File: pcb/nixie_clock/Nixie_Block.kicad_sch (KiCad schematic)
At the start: 25 parts, among them U66 MSD42WT1G, U67 MSD42WT1G, U68 MSD42WT1G, U69 MSD42WT1G, U70 MSD42WT1G, U71 MSD42WT1G, U72 MSD42WT1G, U73 MSD42WT1G, U74 MSD42WT1G, U75 MSD42WT1G, U76 MSD42WT1G, U77 MSD42WT1G

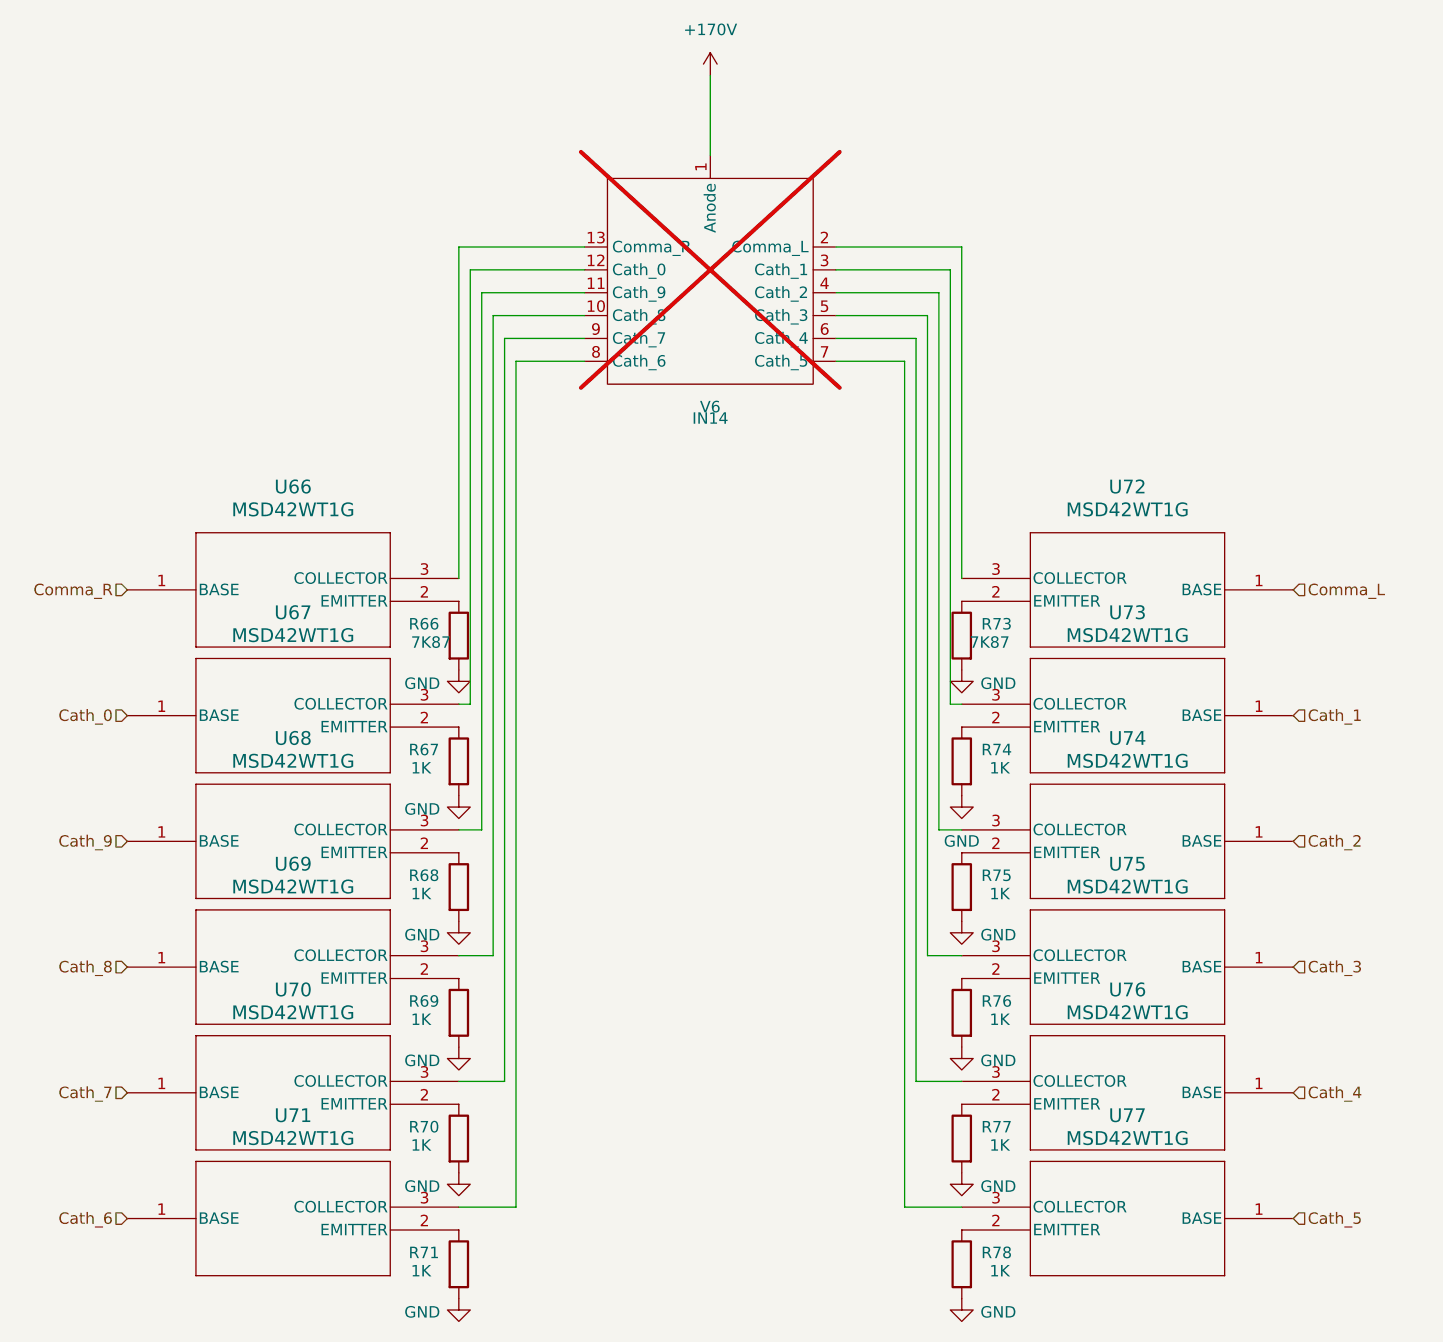
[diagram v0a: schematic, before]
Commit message: pcb changes and breakages need to fix later
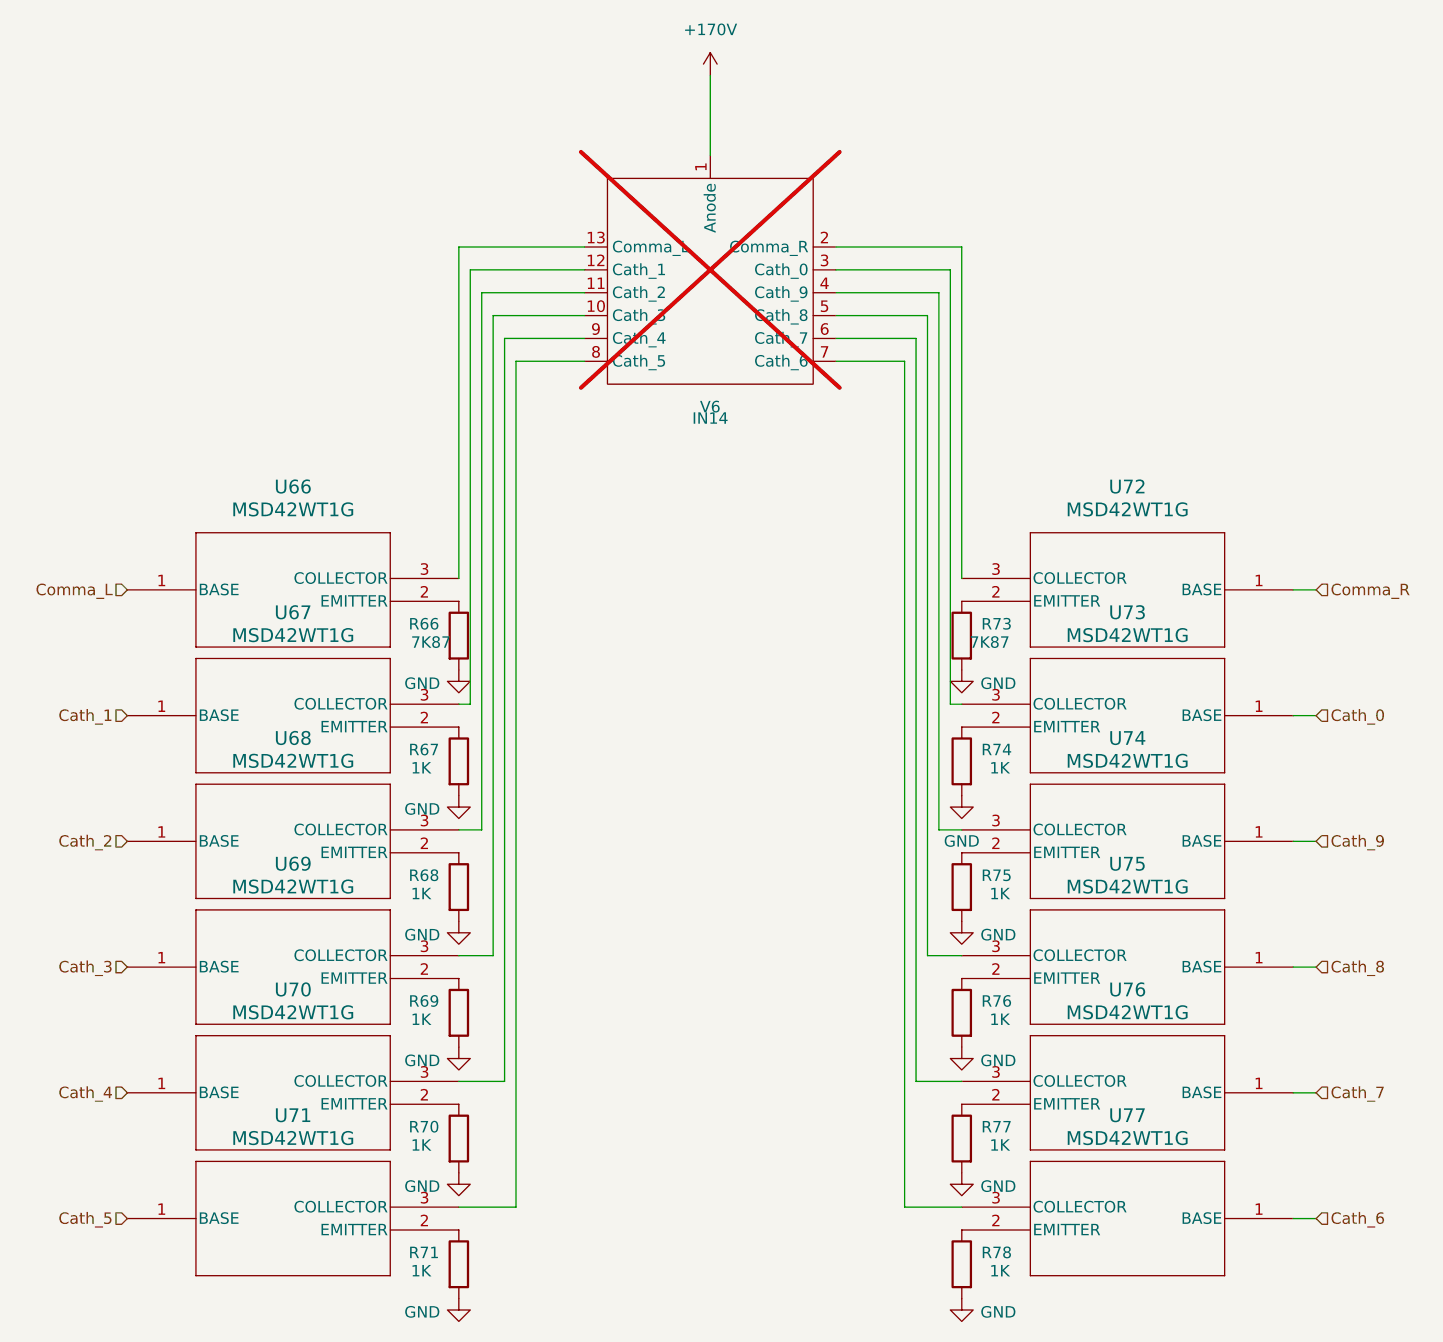
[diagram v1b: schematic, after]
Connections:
- net Cath_0: now also U73.1 (BASE); no longer U67.1 (BASE)
- net Cath_1: now also U67.1 (BASE); no longer U73.1 (BASE)
- net Cath_2: now also U68.1 (BASE); no longer U74.1 (BASE)
- net Cath_3: now also U69.1 (BASE); no longer U75.1 (BASE)
- net Cath_4: now also U70.1 (BASE); no longer U76.1 (BASE)
- net Cath_5: now also U71.1 (BASE); no longer U77.1 (BASE)
- net Cath_6: now also U77.1 (BASE); no longer U71.1 (BASE)
- net Cath_7: now also U76.1 (BASE); no longer U70.1 (BASE)
- net Cath_8: now also U75.1 (BASE); no longer U69.1 (BASE)
- net Cath_9: now also U74.1 (BASE); no longer U68.1 (BASE)
- net Comma_L: now also U66.1 (BASE); no longer U72.1 (BASE)
- net Comma_R: now also U72.1 (BASE); no longer U66.1 (BASE)
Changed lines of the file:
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@@
+	(wire
+		(pts
+			(xy 168.91 133.35) (xy 166.37 133.35)
+		)
+		(stroke
+			(width 0)
+			(type default)
+		)
+	)
 	(wire
 		(pts
@@
 	(wire
 		(pts
+			(xy 168.91 147.32) (xy 166.37 147.32)
+		)
+		(stroke
+			(width 0)
+			(type default)
+		)
+	)
+	(wire
+		(pts
 			(xy 80.01 160.02) (xy 80.01 66.04)
 		)
@@
 	(wire
 		(pts
+			(xy 168.91 161.29) (xy 166.37 161.29)
+		)
+		(stroke
+			(width 0)
+			(type default)
+		)
+	)
+	(wire
+		(pts
+			(xy 168.91 119.38) (xy 166.37 119.38)
+		)
+		(stroke
+			(width 0)
+			(type default)
+		)
+	)
+	(wire
+		(pts
 			(xy 76.2 58.42) (xy 76.2 118.11)
 		)
@@
 	(wire
 		(pts
+			(xy 168.91 91.44) (xy 166.37 91.44)
+		)
+		(stroke
+			(width 0)
+			(type default)
+		)
+	)
+	(wire
+		(pts
+			(xy 168.91 105.41) (xy 166.37 105.41)
+		)
+		(stroke
+			(width 0)
+			(type default)
+		)
+	)
+	(wire
+		(pts
 			(xy 87.63 53.34) (xy 73.66 53.34)
 		)
@@
 	(hierarchical_label "Cath_1"
 		(shape input)
-		(at 166.37 105.41 0)
-		(fields_autoplaced yes)
-		(effects
-			(font
-				(size 1.27 1.27)
-			)
-			(justify left)
+		(at 36.83 105.41 180)
+		(fields_autoplaced yes)
+		(effects
+			(font
+				(size 1.27 1.27)
+			)
+			(justify right)
 		)
 	)
 	(hierarchical_label "Cath_9"
 		(shape input)
+		(at 168.91 119.38 0)
+		(fields_autoplaced yes)
+		(effects
+			(font
+				(size 1.27 1.27)
+			)
+			(justify left)
+		)
+	)
+	(hierarchical_label "Comma_R"
+		(shape input)
+		(at 168.91 91.44 0)
+		(fields_autoplaced yes)
+		(effects
+			(font
+				(size 1.27 1.27)
+			)
+			(justify left)
+		)
+	)
+	(hierarchical_label "Comma_L"
+		(shape input)
+		(at 36.83 91.44 180)
+		(fields_autoplaced yes)
+		(effects
+			(font
+				(size 1.27 1.27)
+			)
+			(justify right)
+		)
+	)
+	(hierarchical_label "Cath_8"
+		(shape input)
+		(at 168.91 133.35 0)
+		(fields_autoplaced yes)
+		(effects
+			(font
+				(size 1.27 1.27)
+			)
+			(justify left)
+		)
+	)
+	(hierarchical_label "Cath_2"
+		(shape input)
 		(at 36.83 119.38 180)
 		(fields_autoplaced yes)
@@
 		)
 	)
-	(hierarchical_label "Comma_R"
-		(shape input)
-		(at 36.83 91.44 180)
-		(fields_autoplaced yes)
-		(effects
-			(font
-				(size 1.27 1.27)
-			)
-			(justify right)
-		)
-	)
-	(hierarchical_label "Comma_L"
-		(shape input)
-		(at 166.37 91.44 0)
-		(fields_autoplaced yes)
-		(effects
-			(font
-				(size 1.27 1.27)
-			)
-			(justify left)
-		)
-	)
-	(hierarchical_label "Cath_8"
+	(hierarchical_label "Cath_7"
+		(shape input)
+		(at 168.91 147.32 0)
+		(fields_autoplaced yes)
+		(effects
+			(font
+				(size 1.27 1.27)
+			)
+			(justify left)
+		)
+	)
+	(hierarchical_label "Cath_0"
+		(shape input)
+		(at 168.91 105.41 0)
+		(fields_autoplaced yes)
+		(effects
+			(font
+				(size 1.27 1.27)
+			)
+			(justify left)
+		)
+	)
+	(hierarchical_label "Cath_5"
+		(shape input)
+		(at 36.83 161.29 180)
+		(fields_autoplaced yes)
+		(effects
+			(font
+				(size 1.27 1.27)
+			)
+			(justify right)
+		)
+	)
+	(hierarchical_label "Cath_4"
+		(shape input)
+		(at 36.83 147.32 180)
+		(fields_autoplaced yes)
+		(effects
+			(font
+				(size 1.27 1.27)
+			)
+			(justify right)
+		)
+	)
+	(hierarchical_label "Cath_3"
 		(shape input)
 		(at 36.83 133.35 180)
@@
 		)
 	)
-	(hierarchical_label "Cath_2"
-		(shape input)
-		(at 166.37 119.38 0)
-		(fields_autoplaced yes)
-		(effects
-			(font
-				(size 1.27 1.27)
-			)
-			(justify left)
-		)
-	)
-	(hierarchical_label "Cath_7"
-		(shape input)
-		(at 36.83 147.32 180)
-		(fields_autoplaced yes)
-		(effects
-			(font
-				(size 1.27 1.27)
-			)
-			(justify right)
-		)
-	)
-	(hierarchical_label "Cath_0"
-		(shape input)
-		(at 36.83 105.41 180)
-		(fields_autoplaced yes)
-		(effects
-			(font
-				(size 1.27 1.27)
-			)
-			(justify right)
-		)
-	)
-	(hierarchical_label "Cath_5"
-		(shape input)
-		(at 166.37 161.29 0)
-		(fields_autoplaced yes)
-		(effects
-			(font
-				(size 1.27 1.27)
-			)
-			(justify left)
-		)
-	)
-	(hierarchical_label "Cath_4"
-		(shape input)
-		(at 166.37 147.32 0)
-		(fields_autoplaced yes)
-		(effects
-			(font
-				(size 1.27 1.27)
-			)
-			(justify left)
-		)
-	)
-	(hierarchical_label "Cath_3"
-		(shape input)
-		(at 166.37 133.35 0)
-		(fields_autoplaced yes)
-		(effects
-			(font
-				(size 1.27 1.27)
-			)
-			(justify left)
-		)
-	)
 	(hierarchical_label "Cath_6"
 		(shape input)
-		(at 36.83 161.29 180)
-		(fields_autoplaced yes)
-		(effects
-			(font
-				(size 1.27 1.27)
-			)
-			(justify right)
-		)
-	)
+		(at 168.91 161.29 0)
+		(fields_autoplaced yes)
+		(effects
+			(font
+				(size 1.27 1.27)
+			)
+			(justify left)
+		)
+	)
